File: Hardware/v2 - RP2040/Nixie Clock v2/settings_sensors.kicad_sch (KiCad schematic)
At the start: 8 parts, among them SW3 SW_DIP_x08, U8 PCF8574A, U9 DS3231MZ

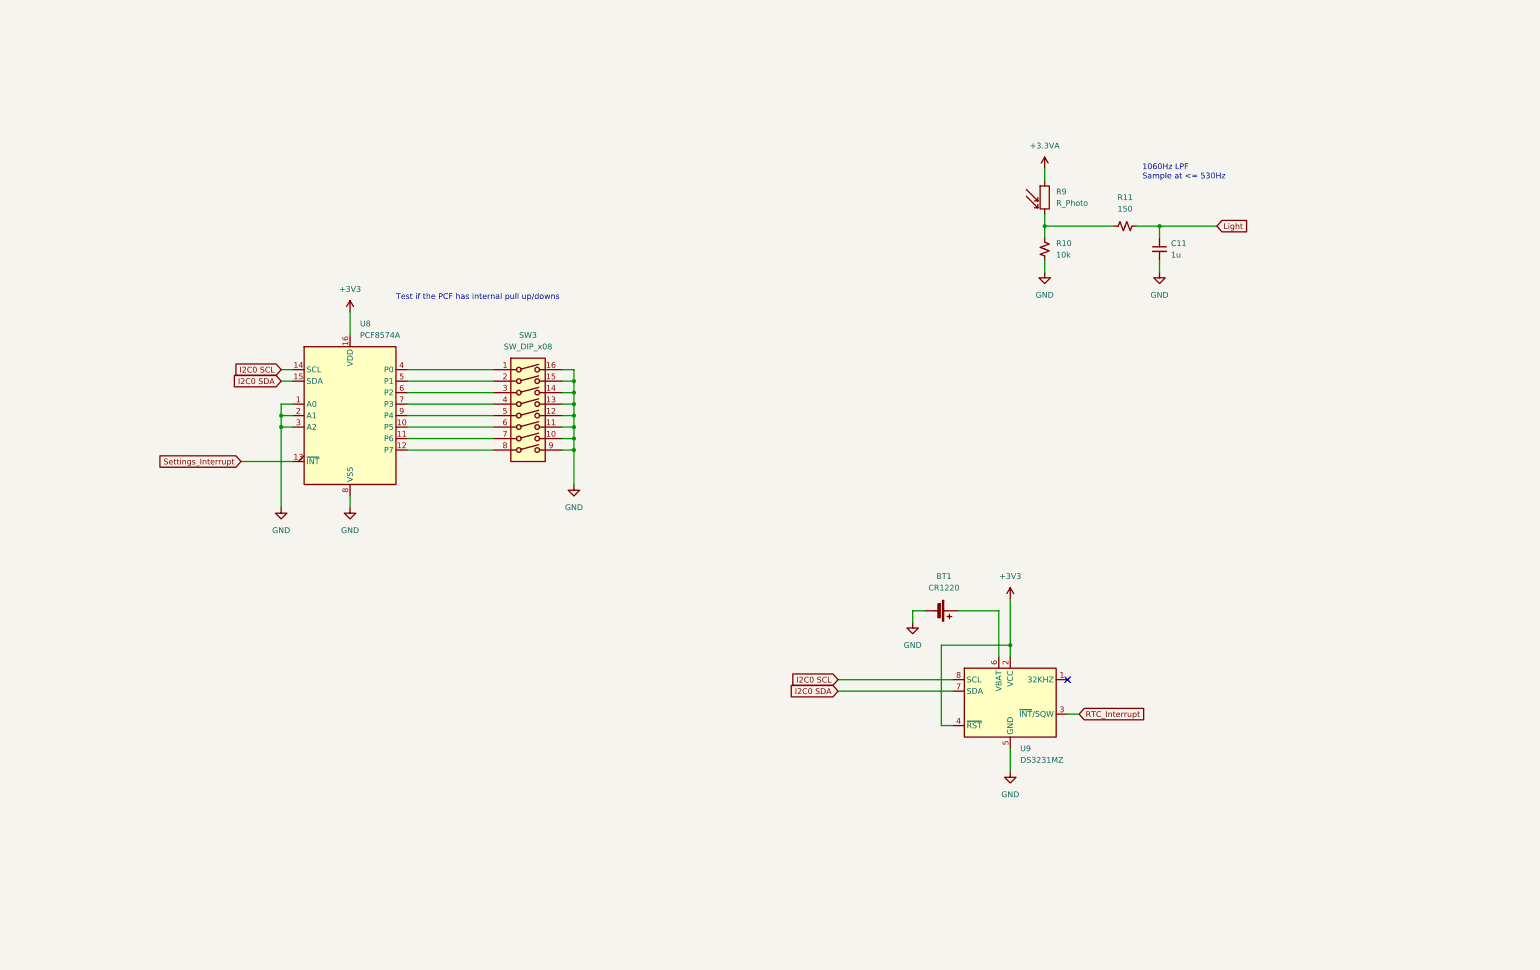
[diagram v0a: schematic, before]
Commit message: Complteted schematic, mergerd schematic on to one sheet, started assigning footprints
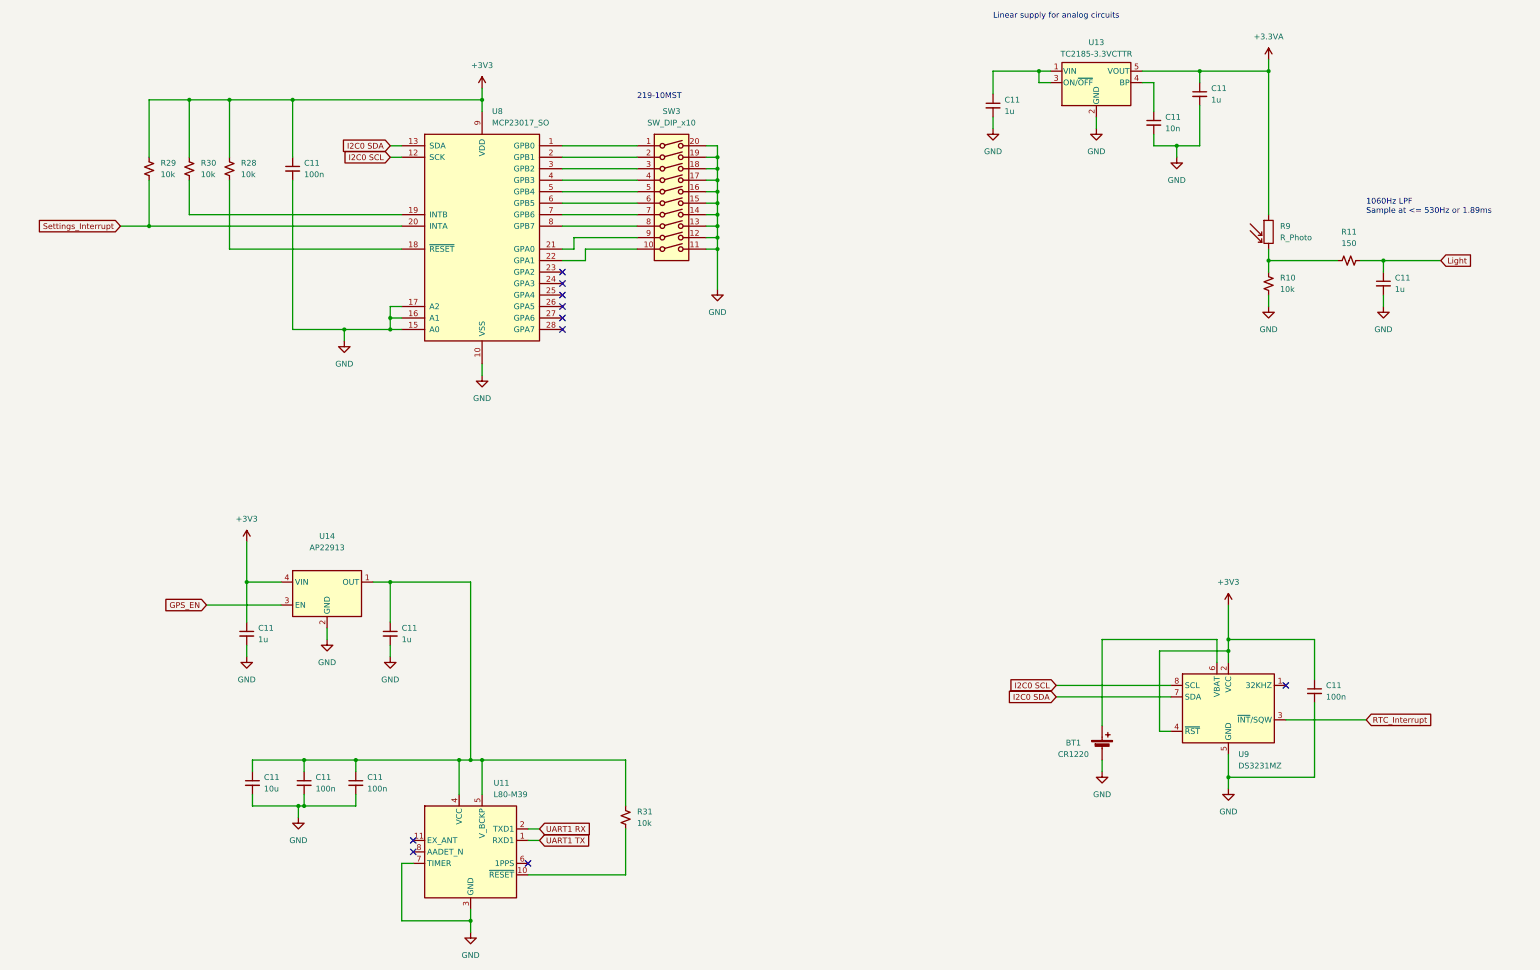
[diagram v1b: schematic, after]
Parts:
- removed SW3: SW_DIP_x08, symbol Switch:SW_DIP_x08
- removed U8: PCF8574A, symbol Interface_Expansion:PCF8574A
- added C11 (x4): 1u, symbol Device:C_Small
- added C11: 10n, symbol Device:C_Small
- added C11 (x4): 100n, symbol Device:C_Small
- added C11: 10u, symbol Device:C_Small
- added R28, R29, R30, R31: 10k, symbol Device:R_Small_US
- added SW3: SW_DIP_x10, symbol Switch:SW_DIP_x10
- added U11: L80-M39, symbol 0_My_Symbols:L80-M39
- added U13: TC2185-3.3VCTTR, Package_TO_SOT_SMD:SOT-23-5, symbol Regulator_Linear:TC2185-3.3VxCTTR
- added U14: AP22913, symbol 0_My_Symbols:AP22913
- added U8: MCP23017_SO, Package_SO:SOIC-28W_7.5x17.9mm_P1.27mm, symbol Interface_Expansion:MCP23017_SO
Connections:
- net +3.3VA: now also C11.1, U13.5 (VOUT)
- net +3V3: now also C11.1, C11.1, C11.1, R28.1, R29.1, R30.1, U14.4 (VIN), U14.6 (VIN), U8.9 (VDD)
- net GND: now also C11.2, C11.2, C11.2, C11.2, C11.2, C11.2, C11.2, C11.2, C11.2, C11.2, SW3.11, SW3.12, SW3.13, SW3.14, SW3.15, SW3.16, SW3.17, SW3.18, SW3.19, SW3.20, U11.12 (GND), U11.3 (GND), U11.7 (TIMER), U13.2 (GND), U14.2 (GND), U14.5 (GND), U8.10 (VSS), U8.15 (A0), U8.16 (A1), U8.17 (A2)
- net I2C0 SCL: now also U8.12 (SCK)
- net I2C0 SDA: now also U8.13 (SDA)
- net Settings_Interrupt: now also R29.2, U8.20 (INTA)
- new net: SW3.1, U8.1 (GPB0)
- new net: SW3.10, U8.22 (GPA1)
- new net: SW3.2, U8.2 (GPB1)
- new net: SW3.3, U8.3 (GPB2)
- new net: SW3.4, U8.4 (GPB3)
- new net: SW3.5, U8.5 (GPB4)
- new net: SW3.6, U8.6 (GPB5)
- new net: SW3.7, U8.7 (GPB6)
- new net: SW3.8, U8.8 (GPB7)
- new net: SW3.9, U8.21 (GPA0)
- new net: R28.2, U8.18 (~{RESET})
- new net: R30.2, U8.19 (INTB)
- new net: C11.1, U13.4 (BP)
- new net: C11.1, C11.1, C11.1, C11.1, R31.1, U11.4 (VCC), U11.5 (V_BCKP), U14.1 (OUT)
- new net: R31.2, U11.10 (~{RESET})
- new net: C11.1, U13.1 (VIN), U13.3 (ON/~{OFF})
- new net GPS_EN: U14.3 (EN)
- new net UART1 RX: U11.2 (TXD1)
- new net UART1 TX: U11.1 (RXD1)
- no-connect marks 1 -> 10
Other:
- note added: "1060Hz LPF Sample at <= 530Hz or 1.89ms"
- note added: "219-10MST"
- note added: "Linear supply for analog circuits"
- note removed: "1060Hz LPF Sample at <= 530Hz"
- note removed: "Test if the PCF has internal pull up/downs"
- moved on the sheet: BT1, C11, R10, R11, R9, U9
